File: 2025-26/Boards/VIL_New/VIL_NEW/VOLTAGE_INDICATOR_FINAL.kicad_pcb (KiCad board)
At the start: 2 copper layers, 47.1 x 53.3 mm, 13 parts, among them Q2 UJ3N065080K3S

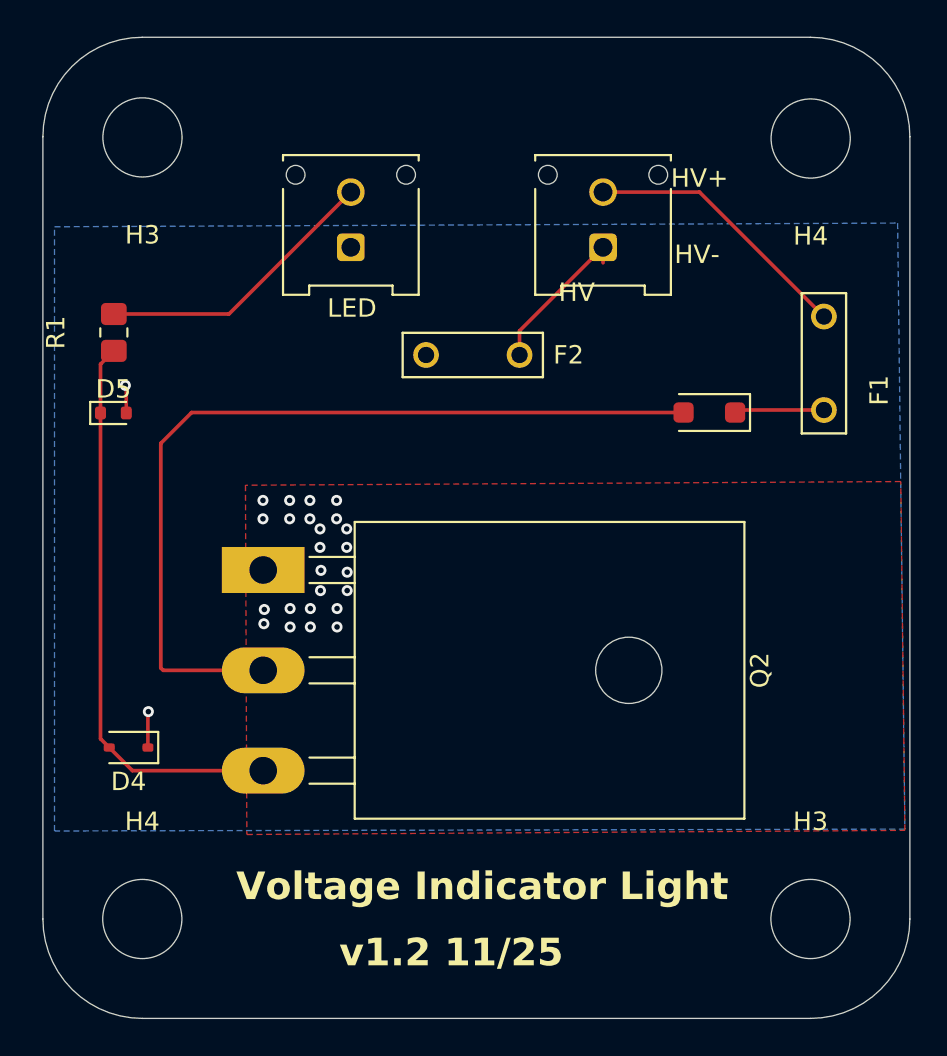
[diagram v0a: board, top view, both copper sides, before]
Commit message: added updated Relay, VIL, and RML
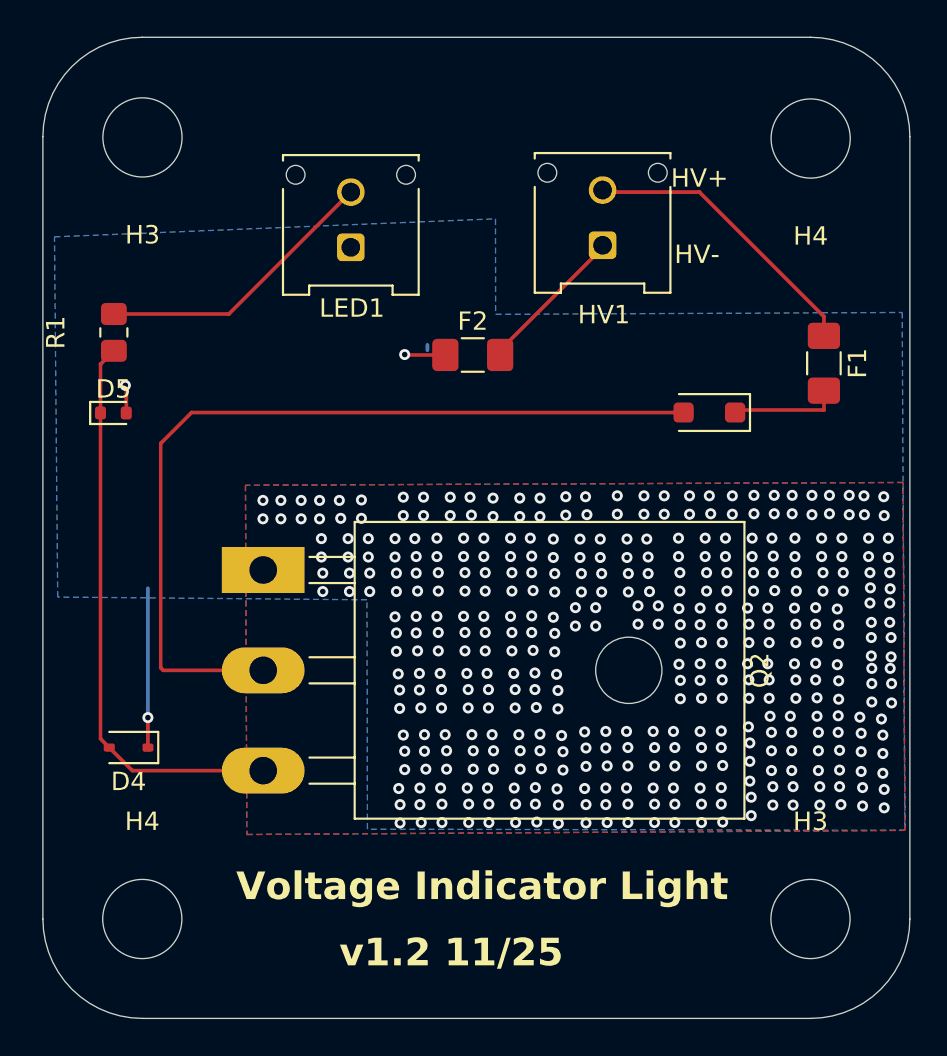
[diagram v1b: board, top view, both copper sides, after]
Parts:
- F1, F2: footprint Library:FUSE_BK_PCS -> Fuse:Fuse_1206_3216Metric_Pad1.42x1.75mm_HandSolder
- moved HV1 0.11 mm to (143.7, 79.4)
- renumbered HV to HV1, LED to LED1
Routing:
- net /HV-_fused: track 5.12 -> 14.0 mm, vias 26 -> 411
- net /HV+_fused: track 4.88 -> 5.93 mm
- net /HV+: track 14.8 -> 15.9 mm

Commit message: VIL fixes after kaboom
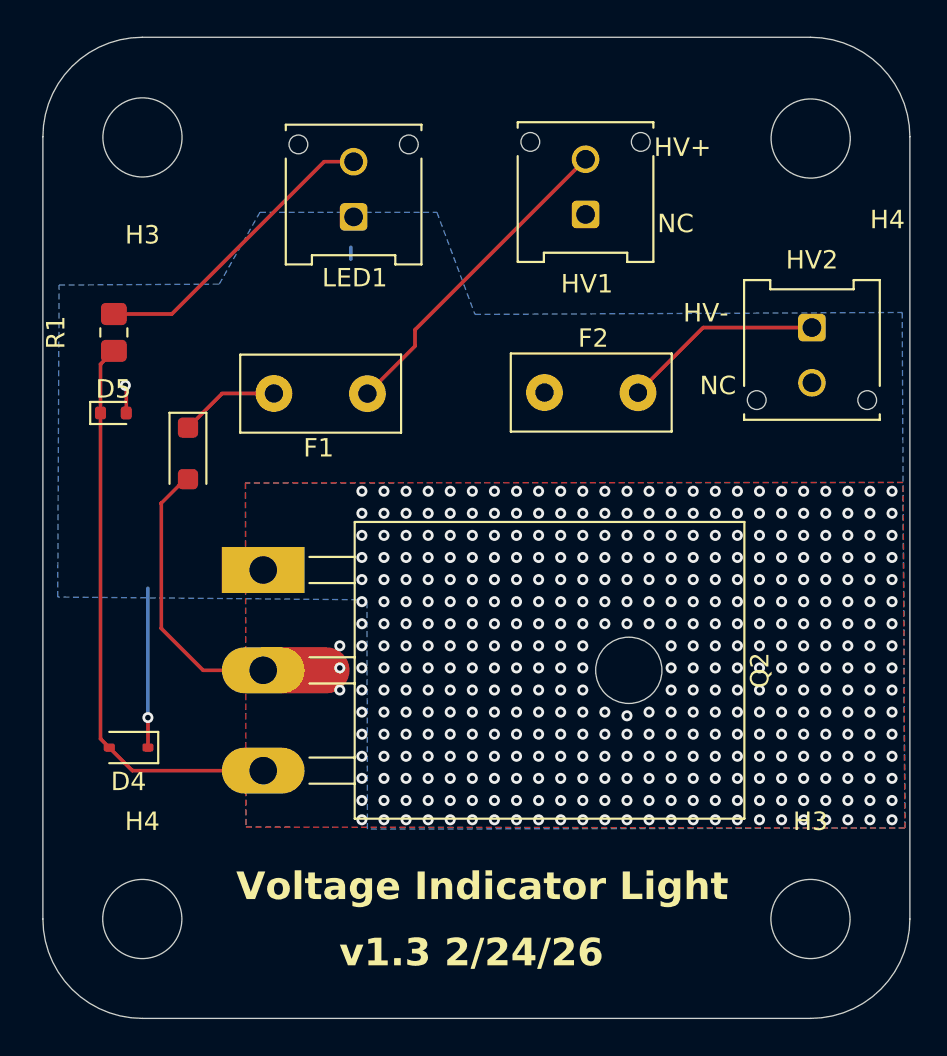
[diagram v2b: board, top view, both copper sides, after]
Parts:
- added HV2: 043045-0212, Connector_Molex:Molex_Micro-Fit_3.0_43045-0212_2x01_P3.00mm_Vertical, F.Cu at (155.1, 83.9)
- F1, F2: footprint Fuse:Fuse_1206_3216Metric_Pad1.42x1.75mm_HandSolder -> Fuse:Fuse_Littelfuse_395Series
- moved D3 28.4 mm to (121.2, 90.7), turned to -90 degrees
- moved F1 24.9 mm to (130.9, 87.5), turned to 180 degrees
- moved F2 4.40 mm to (140.5, 87.4)
- moved HV1 1.91 mm to (142.8, 77.7)
- moved LED1 1.66 mm to (130.2, 77.8)
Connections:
- HV1 pad 1: /HV- -> unconnected-(HV1-Pin_1-Pad1)
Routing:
- net Net-(D3-A): track 48.8 -> 20.7 mm, vias 0 -> 394
- net /HV-_fused: track 14.0 -> 10.9 mm, vias 411 -> 2
- net /HV-: track 8.16 -> 10.9 mm
- net /HV+: track 15.9 -> 17.6 mm
- net /LED+: track 15.6 -> 16.5 mm
- added copper zone on B.Cu, net Net-(D3-A)
- added copper zone on F.Cu, net Net-(D3-A)
- removed copper zone on F.Cu, net /HV-_fused
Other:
- board text added: "NC"
- board text added: "v1.3 2/24/26"
- board text removed: "v1.2 11/25"
